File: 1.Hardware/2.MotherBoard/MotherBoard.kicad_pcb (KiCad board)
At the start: 2 copper layers, 56.7 x 59 mm, 72 parts, among them J1 9-Axis, J10 GPS, J4 WIRELESS, J5 MOTOR, J6 FLY_WHEEL, J7 MOTOR, J8 MOTOR_BACK, J9 SERVO, Q1 S8050, SW1 SW_SPDT, U1 ME3116, U2 RT9013-33GB, U3 ME3116, U4 SCEP_CH32V3, U5 MT9V034

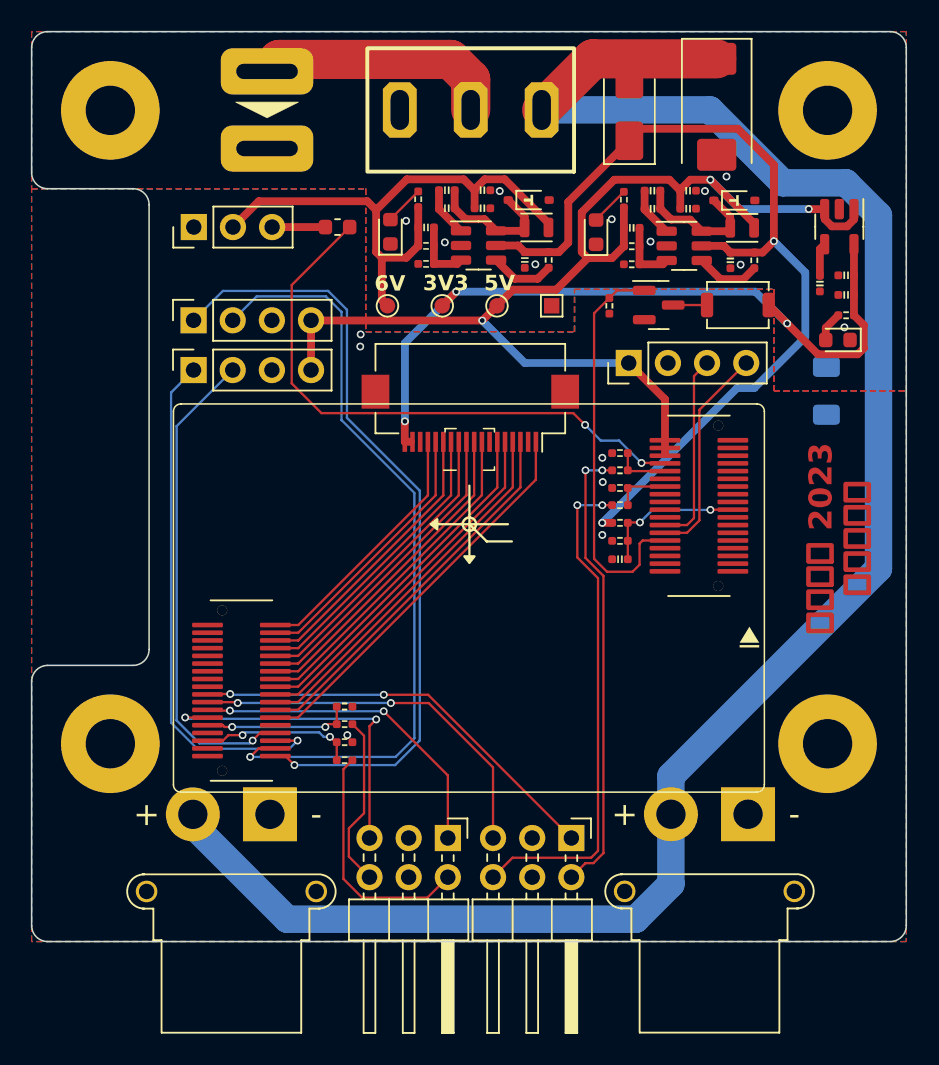
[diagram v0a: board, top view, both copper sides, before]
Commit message: MotherBoard v1.1 and AIO driver board sch
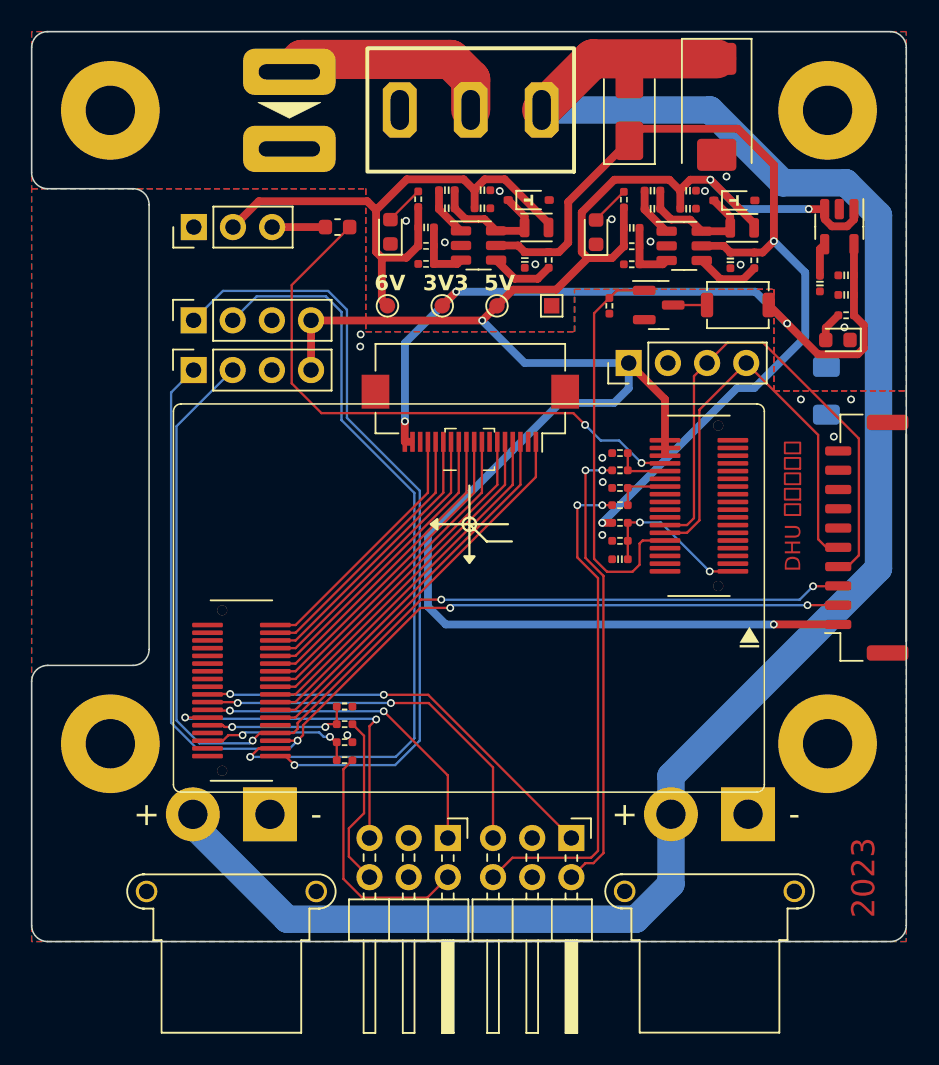
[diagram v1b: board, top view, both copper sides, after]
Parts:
- added J2: NEO3, Connector_JST:JST_GH_SM10B-GHS-TB_1x10-1MP_P1.25mm_Horizontal, F.Cu at (78.9, 30.9)
- moved J? 1.45 mm to (41.5, 3.15)
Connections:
- U4 pad 64: /BATTERY -> unconnected-(U4-PB1-Pad64)
- U4 pad 72: unconnected-(U4-PA7-Pad72) -> /BATTERY
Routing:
- net +5V: track 75.8 -> 126.1 mm, vias 3 -> 4
- net /UART8_RX: track 31.5 -> 72.2 mm, vias 1 -> 3
- net /UART8_TX: track 34.0 -> 73.1 mm, vias 1 -> 3
- net /AUX_SCL: track 12.5 -> 34.7 mm
- net /AUX_SDA: track 14.0 -> 28.9 mm
- net VBUS: track 16.0 -> 14.6 mm
- net /BATTERY: track 9.53 -> 10.5 mm
- net GND: vias 6 -> 9
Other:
- board text added: "2023"
- board text added: "DHU 敏感词汇队"
- board text removed: "东华大学 2023 敏感词汇队"
